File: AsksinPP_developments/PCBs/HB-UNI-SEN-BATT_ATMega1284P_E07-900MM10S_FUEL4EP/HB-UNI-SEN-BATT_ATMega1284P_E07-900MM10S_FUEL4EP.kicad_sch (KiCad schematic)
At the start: 60 parts, among them J1 Conn_01x02, J10 charge, J11 ePaper connector, J12 FTDI Debuger, J13 U.FL connector, J2 Conn_01x02, J3 Conn_01x02, J4 Conn_01x02, J5 ISP Programmer, J6 Conn_01x04, J7 Conn_01x04, J8 Conn_01x04, J9 Conn_01x04, Q1 IRLU024N, SW1 Config button, SW2 Reset button, U1 ATmega1284P-AU, U2 TPS61221DCK, Y1 8MHz

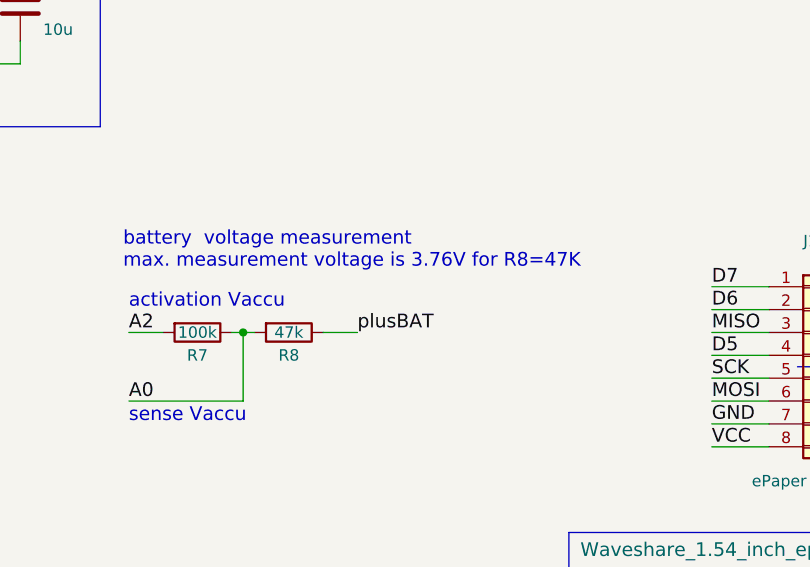
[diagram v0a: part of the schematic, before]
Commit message: PCBs: HB_TH_Sensor_SHT45_AllInOne_FUEL4EP and HB-UNI-SEN-BATT_ATMega1284P_E07-900MM10S_FUEL4EP: fix of wrong LCSC part numbers
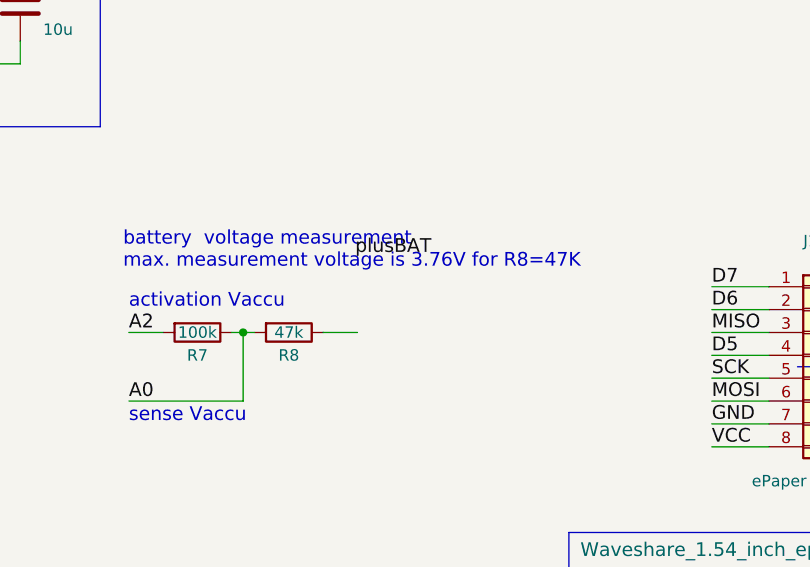
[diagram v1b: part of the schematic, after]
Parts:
- C1: LCSC C7171 -> C15525; TYPE CASE-A_3216 -> 0402
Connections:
- net plusBAT: no longer R8.1
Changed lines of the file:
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@@
   (title_block
     (title "HB-UNI-SEN-BATT_ATMega1284P_E07-900MM10S_FUEL4EP")
-    (date "2023-09-13")
-    (rev "1.0")
+    (date "2024-01-08")
+    (rev "1.1")
     (company "FUEL4EP")
     (comment 1 "Creative Commons License, non-commercial")
@@
     (effects (font (size 1.524 1.524)) (justify left bottom))
   )
-  (label "plusBAT" (at 212.725 79.375 0)
+  (label "plusBAT" (at 212.471 70.993 0)
     (effects (font (size 1.524 1.524)) (justify left bottom))
   )
@@
       (effects (font (size 1.27 1.27)) hide)
     )
-    (property "TYPE" "CASE-A_3216" (id 4) (at 119.38 92.71 0)
-      (effects (font (size 1.27 1.27)) hide)
-    )
-    (property "LCSC" "C7171" (id 5) (at 119.38 92.71 0)
-      (effects (font (size 1.27 1.27)) hide)
-    )
+    (property "TYPE" "0402" (id 4) (at 119.38 92.71 0)
+      (effects (font (size 1.27 1.27)) hide)
+    )
+    (property "LCSC" "C15525" (id 5) (at 119.38 92.71 0)
+      (effects (font (size 1.27 1.27)) hide)
+    )

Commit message: PCBs: documentation updates / PCBs: HB-UNI-SEN-BATT_ATMega1284P_E07-868MS10_FUEL4EP, HB-UNI-SEN-BATT_ATMega1284P_E07-868MS10_FRAM_FUEL4EP, HB-UNI-SEN-BATT_ATMega1284P_E07-900MM10S_FUEL4EP: fix of wrong LCSC number for R7
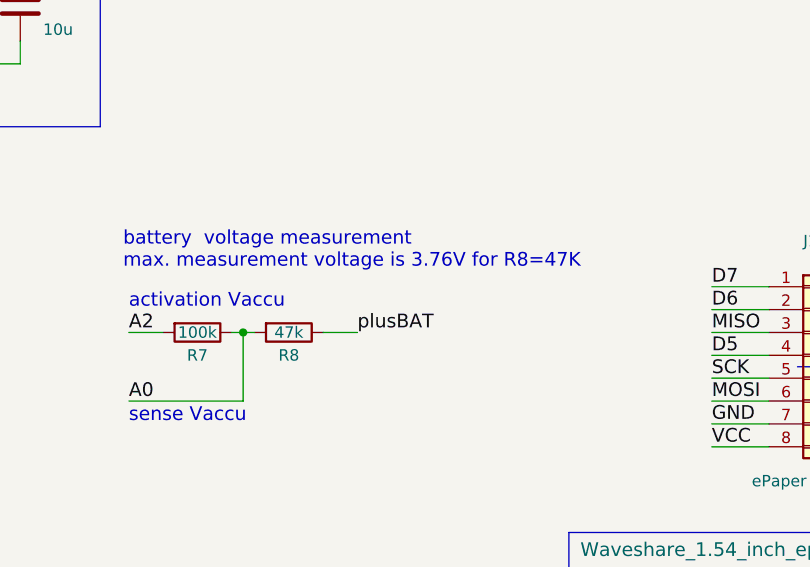
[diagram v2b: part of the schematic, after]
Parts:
- R7: LCSC C25271 -> C149504
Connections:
- net plusBAT: now also R8.1
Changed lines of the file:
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@@
   (title_block
     (title "HB-UNI-SEN-BATT_ATMega1284P_E07-900MM10S_FUEL4EP")
-    (date "2024-01-08")
-    (rev "1.1")
+    (date "2024-02-17")
+    (rev "1.3")
     (company "FUEL4EP")
     (comment 1 "Creative Commons License, non-commercial")
@@
     (effects (font (size 1.524 1.524)) (justify left bottom))
   )
-  (label "plusBAT" (at 212.471 70.993 0)
+  (label "plusBAT" (at 212.725 79.375 0)
     (effects (font (size 1.524 1.524)) (justify left bottom))
   )
@@
       (effects (font (size 1.27 1.27)) hide)
     )
-    (property "Datasheet" "https://datasheet.lcsc.com/lcsc/1809140123_UNI-ROYAL-Uniroyal-Elec-0805W8F100KT5E_C25271.pdf" (id 3) (at 194.945 79.375 0)
+    (property "Datasheet" "https://datasheet.lcsc.com/lcsc/2205312316_UNI-ROYAL-Uniroyal-Elec-0805W8F1003T5E_C149504.pdf" (id 3) (at 194.945 79.375 0)
       (effects (font (size 1.27 1.27)) hide)
     )
@@
       (effects (font (size 1.27 1.27)) hide)
     )
-    (property "LCSC" "C25271" (id 5) (at 194.945 79.375 0)
-      (effects (font (size 1.27 1.27)) hide)
-    )
+    (property "LCSC" "C149504" (id 5) (at 194.945 79.375 0)
+      (effects (font (size 1.27 1.27)) hide)
+    )

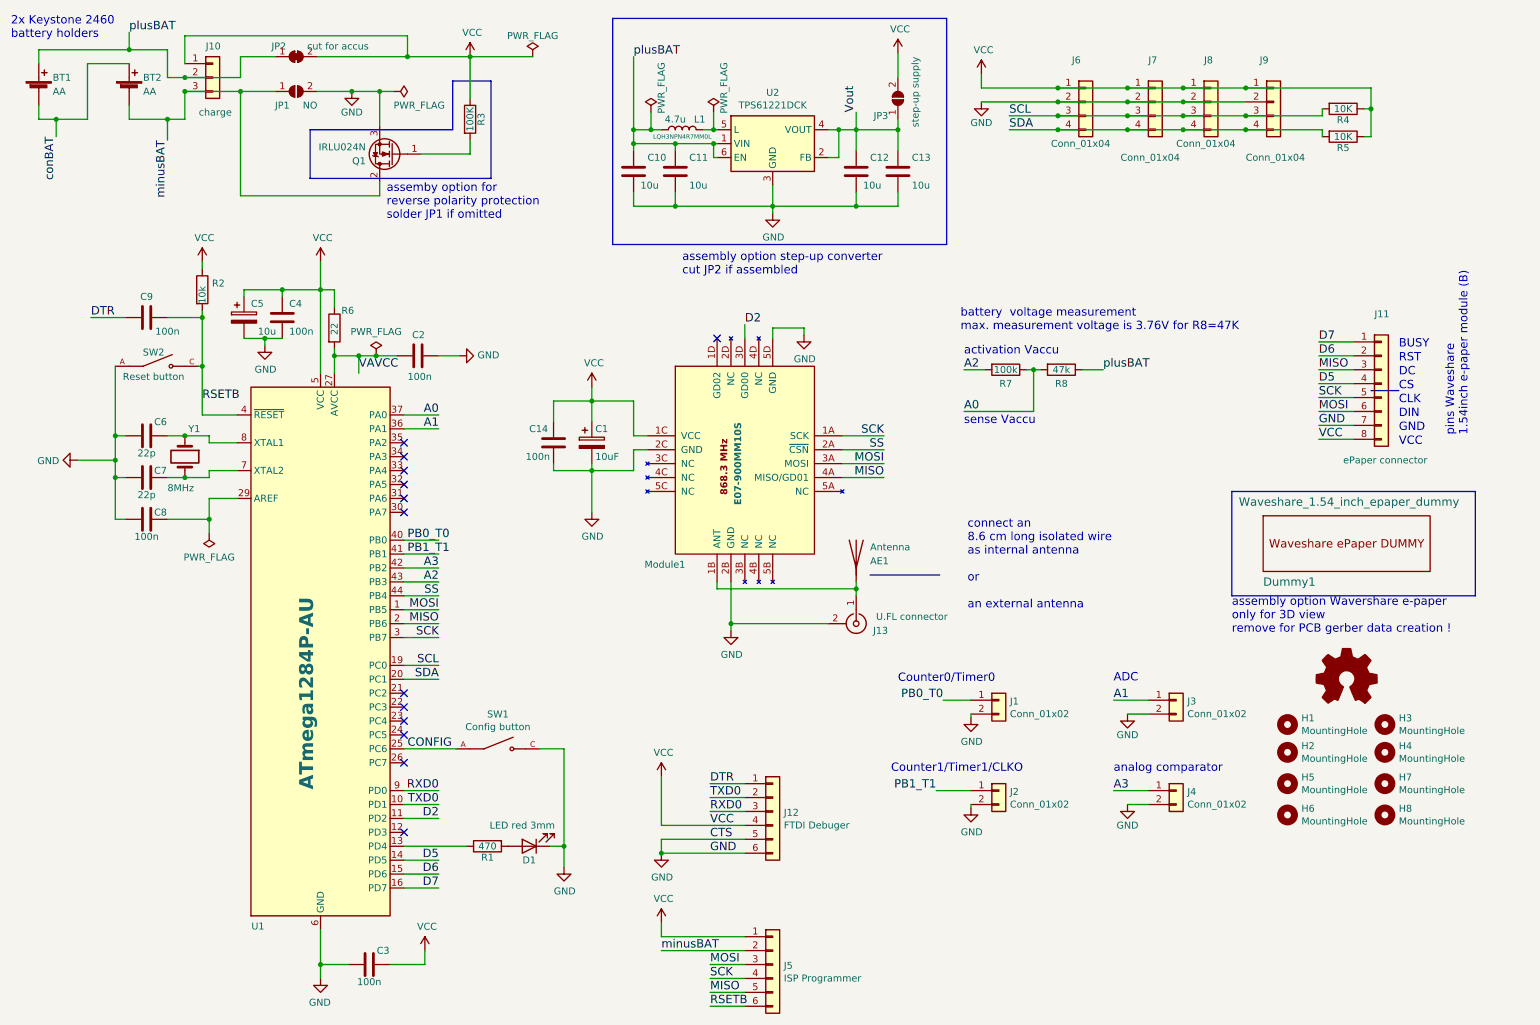
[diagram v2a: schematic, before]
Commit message: PCBs/HB-UNI-SEN-BATT_ATMega1284P_E07-900MM10S_FUEL4EP: migration to KiCAD 8, LCSC fixes; PCBs/HB-UNI-SEN-BATT_ATMega1284P_E07-868MS10_FUEL4EP: BOM update
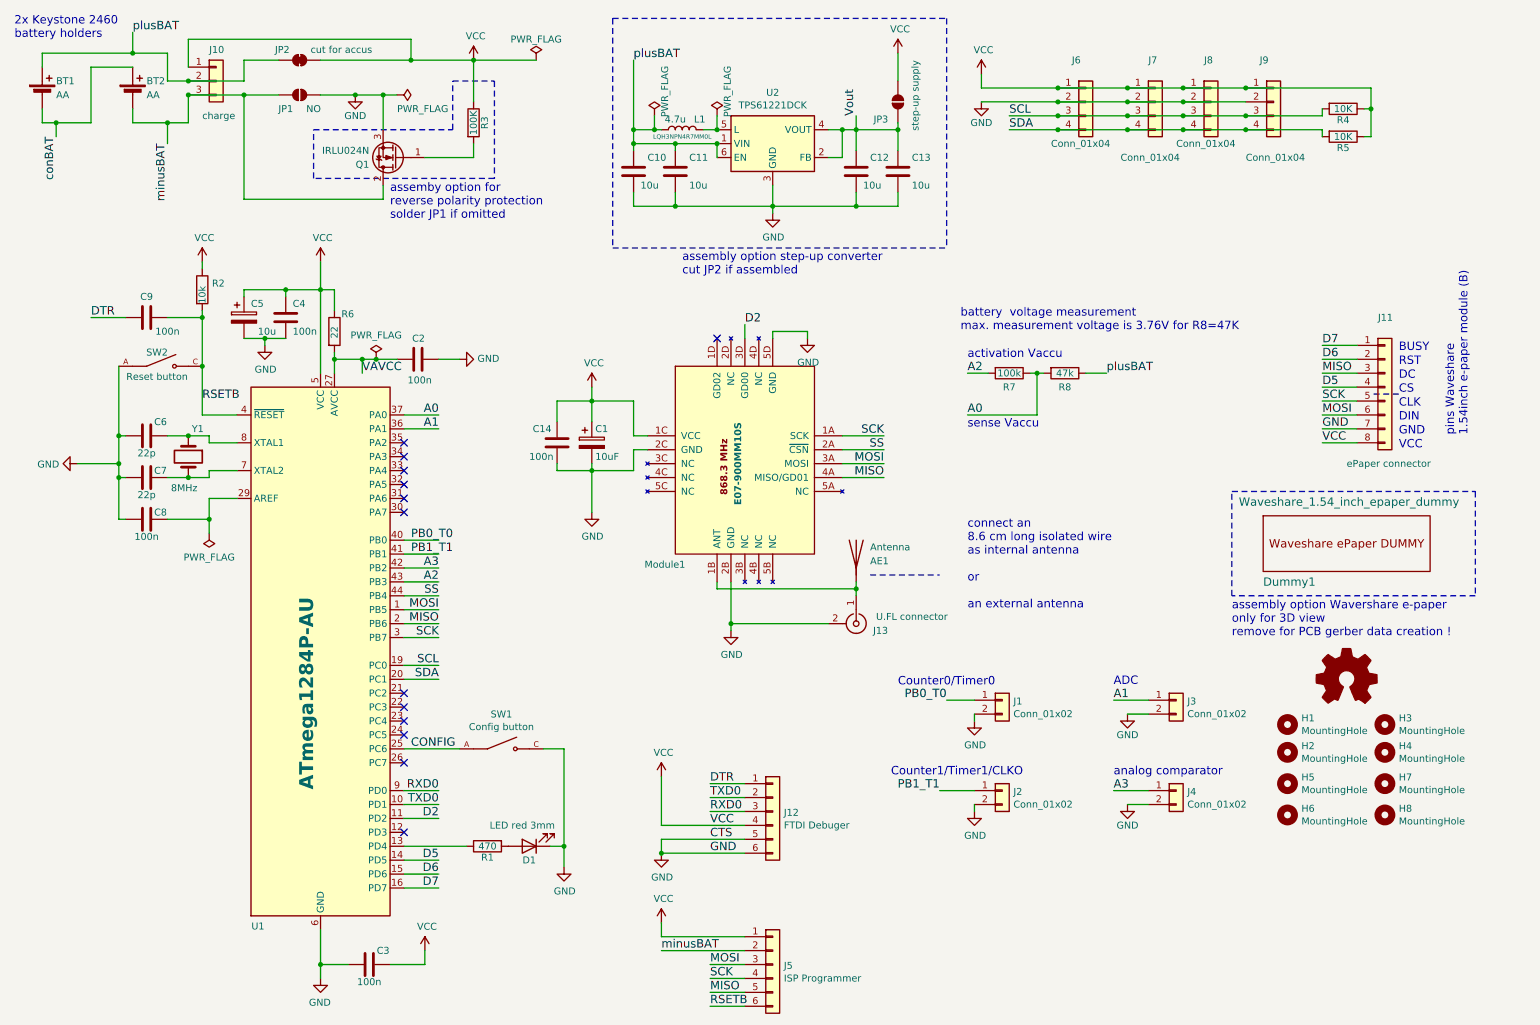
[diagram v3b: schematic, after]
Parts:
- C14: LCSC (none) -> C338011; TYPE (none) -> 0402
- R2: LCSC C17733 -> C17414
- R4, R5: LCSC C101933 -> C17414; TYPE R0805 -> 0805
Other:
- moved on the sheet: BT1, BT2, C14, C2, C4, J1, J10, J11, J2, Q1, R3, R6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
